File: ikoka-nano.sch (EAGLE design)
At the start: 6 parts, among them IC1 E22-900M22S, J1 Vertical Qwiic Connector, J2 Vertical Qwiic Connector, J3 Vertical Qwiic Connector

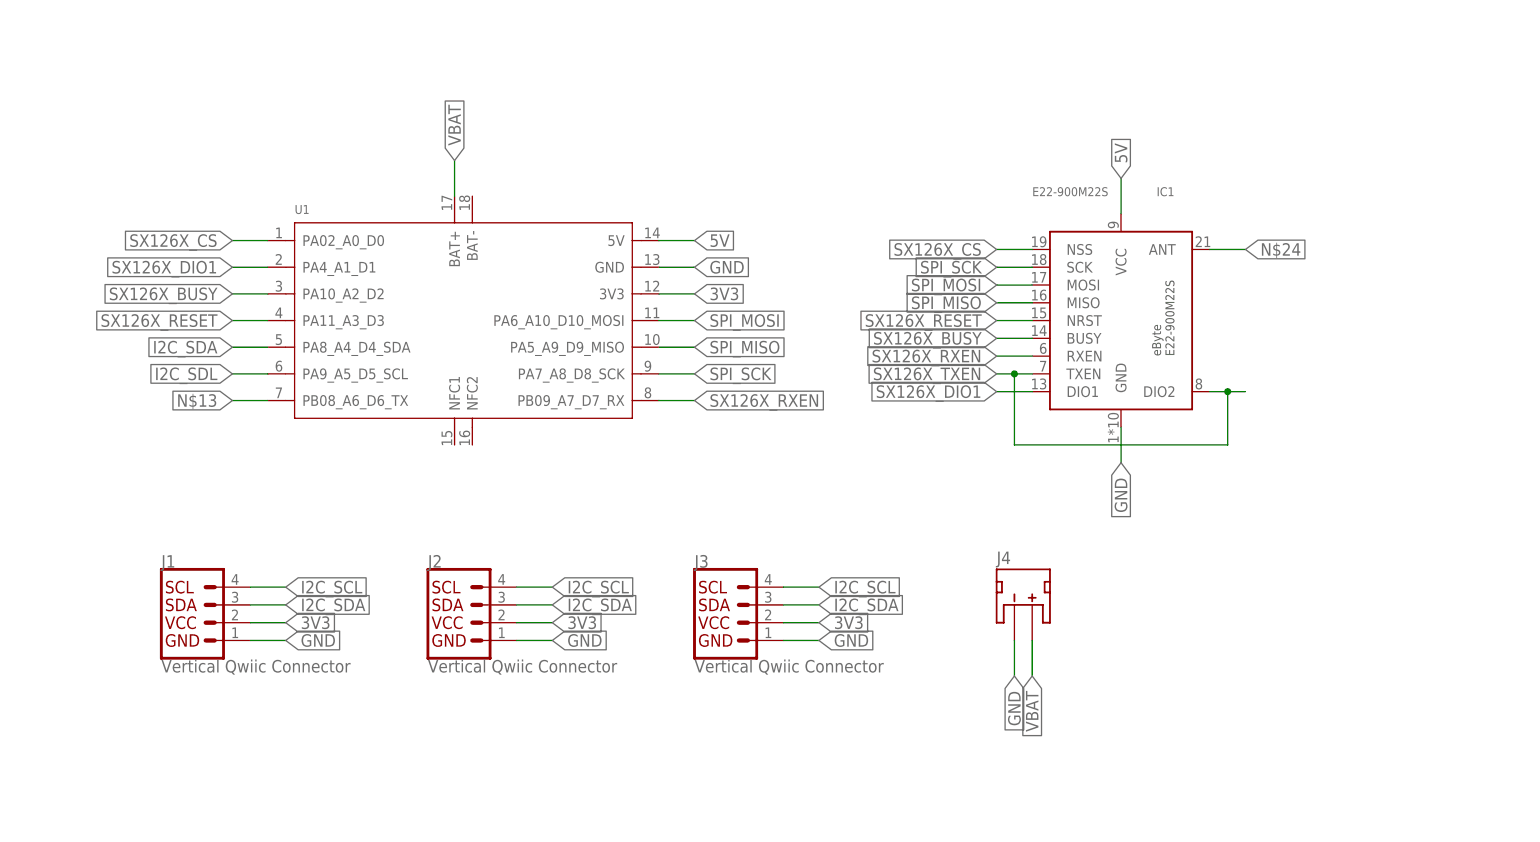
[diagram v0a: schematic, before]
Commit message: Redesign board because the E22-900M22S footprint from SnapMagic was much smaller than the actual module size; add solar 5V connector; reduce Qwiic connectors to just one.
Signed-off-by: Andrew Yong <me@ndoo.sg>
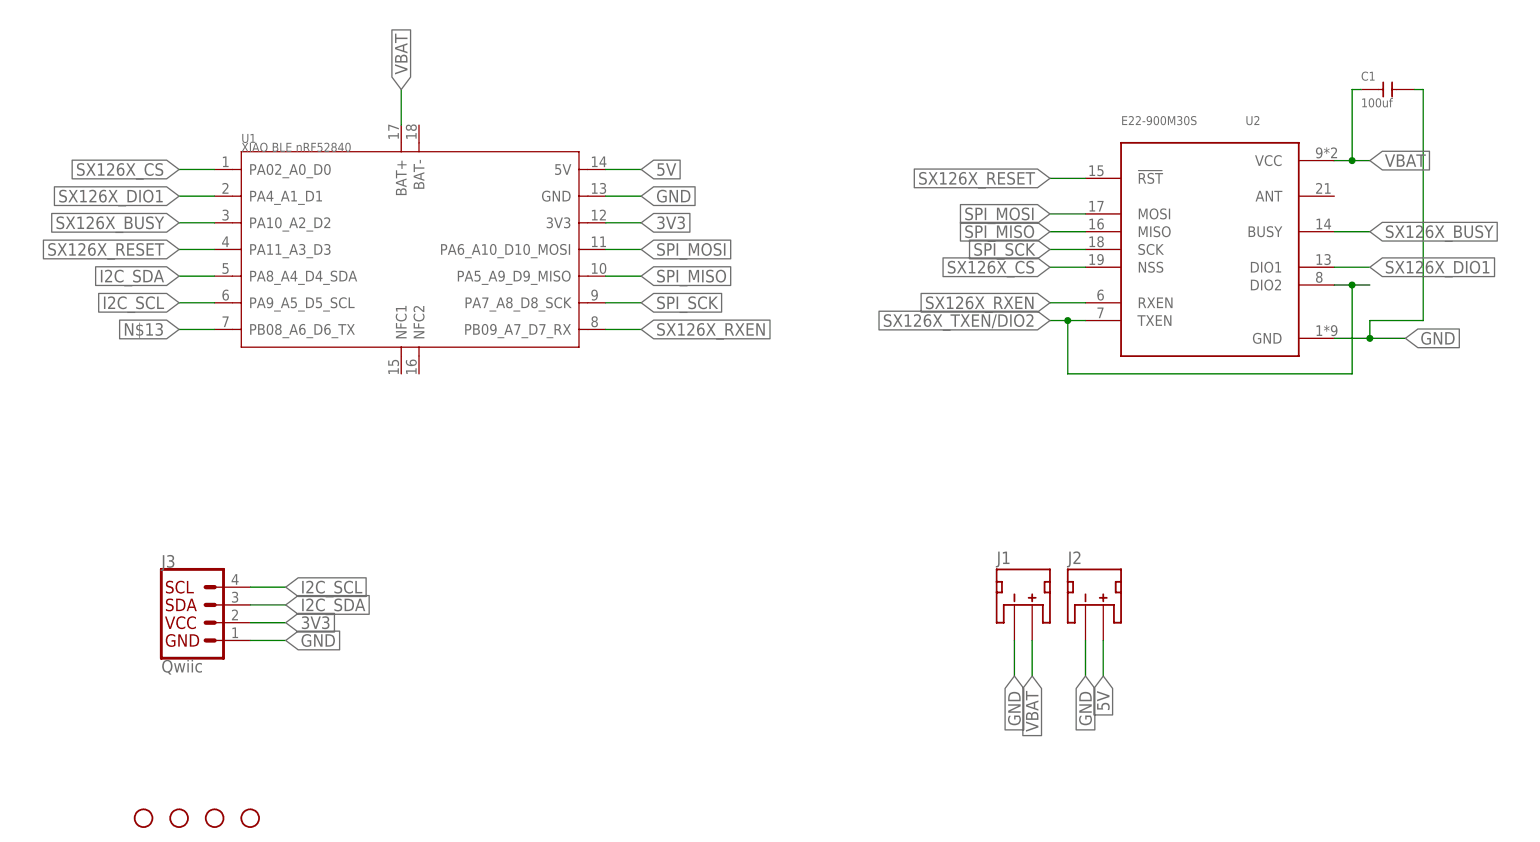
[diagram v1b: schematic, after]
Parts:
- removed IC1: E22-900M22S, E22-900M22S:E22-900M22S
- removed J4: (no value), SparkFun-Connectors:JST_2MM_MALE
- added C1: 100uf, OPL_Capacitor:CERAMIC-100UF-6.3V-20%-X5R(1206)
- added H1, H2, H3, H4: STAND-OFF, SparkFun-Hardware:STAND-OFF
- added U2: E22-900M30S, E22-900M30S:E22-900M30S
- J1: value Vertical Qwiic Connector -> LiPo 1S; device SparkFun-Connectors:QWIIC_CONNECTOR -> SparkFun-Connectors:JST_2MM_MALE
- J2: value Vertical Qwiic Connector -> Solar ≤6.45V; device SparkFun-Connectors:QWIIC_CONNECTOR -> SparkFun-Connectors:JST_2MM_MALE
- J3: value Vertical Qwiic Connector -> Qwiic; device SparkFun-Connectors:QWIIC_CONNECTOR -> SparkFun-Connectors:QWIIC_CONNECTORJS-1MM
- U1: value (none) -> XIAO BLE nRF52840
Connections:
- removed net I2C_SDL: U1.PA9_A5_D5_SCL
- removed net N$24: IC1.ANT
- removed net SX126X_TXEN: IC1.DIO2, IC1.TXEN
- new net SX126X_TXEN/DIO2: U2.DIO2, U2.TXEN
- net 3V3: no longer J1.2, J2.2
- net 5V: now also J2.+; no longer IC1.VCC
- net GND: now also C1.2, J1.-, J2.-, U2.GND; no longer IC1.GND, J1.1, J2.1, J4.-
- net I2C_SCL: now also U1.PA9_A5_D5_SCL; no longer J1.4, J2.4
- net I2C_SDA: no longer J1.3, J2.3
- net SPI_MISO: now also U2.MISO; no longer IC1.MISO
- net SPI_MOSI: now also U2.MOSI; no longer IC1.MOSI
- net SPI_SCK: now also U2.SCK; no longer IC1.SCK
- net SX126X_BUSY: now also U2.BUSY; no longer IC1.BUSY
- net SX126X_CS: now also U2.NSS; no longer IC1.NSS
- net SX126X_DIO1: now also U2.DIO1; no longer IC1.DIO1
- net SX126X_RESET: now also U2.!RST; no longer IC1.NRST
- net SX126X_RXEN: now also U2.RXEN; no longer IC1.RXEN
- net VBAT: now also C1.1, J1.+, U2.VCC; no longer J4.+
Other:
- moved on the sheet: J3, U1
